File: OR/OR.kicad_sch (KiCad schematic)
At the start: 7 parts, among them J1 AudioJack2_SwitchT, J2 AudioJack2_SwitchT, J3 AudioJack2_SwitchT, Q1 BSS84, Q2 BSS84, Q3 BSS84, Q4 BSS84

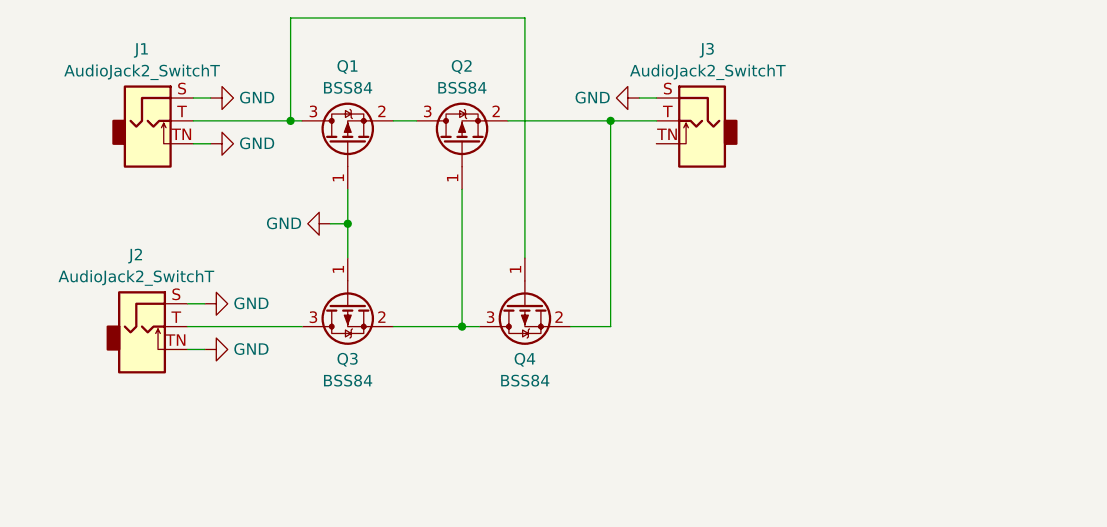
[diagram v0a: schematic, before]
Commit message: Make OR gate lossless
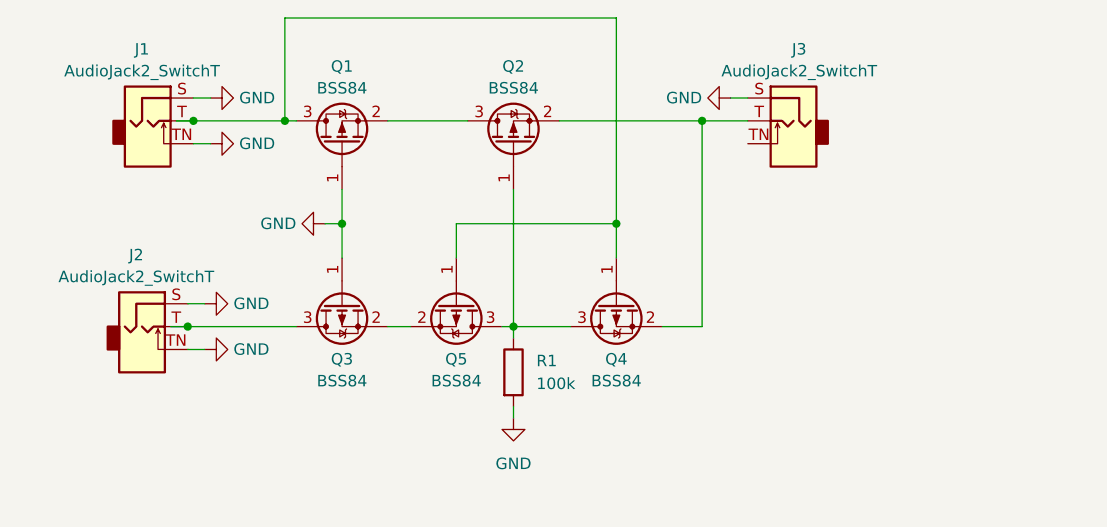
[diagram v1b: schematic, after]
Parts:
- added Q5: BSS84, Package_TO_SOT_SMD:SOT-23, symbol Transistor_FET:BSS84
- added R1: 100k, symbol Device:R
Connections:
- net GND: now also R1.2
- net at J1.T, Q1.3 (D), Q4.1 (G): now also Q5.1 (G)
- net at Q2.1 (G), Q4.3 (D): now also Q5.3 (D), R1.1; no longer Q3.2 (S)
- new net: Q3.2 (S), Q5.2 (S)
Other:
- moved on the sheet: J3, Q1, Q2, Q3, Q4

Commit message: Increase impedance
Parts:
- R1: value 100k -> 1M
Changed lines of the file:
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@@
       (effects (font (size 1.27 1.27)) (justify left))
     )
-    (property "Value" "100k" (at 168.91 96.52 0)
+    (property "Value" "1M" (at 168.91 96.52 0)
       (effects (font (size 1.27 1.27)) (justify left))
     )

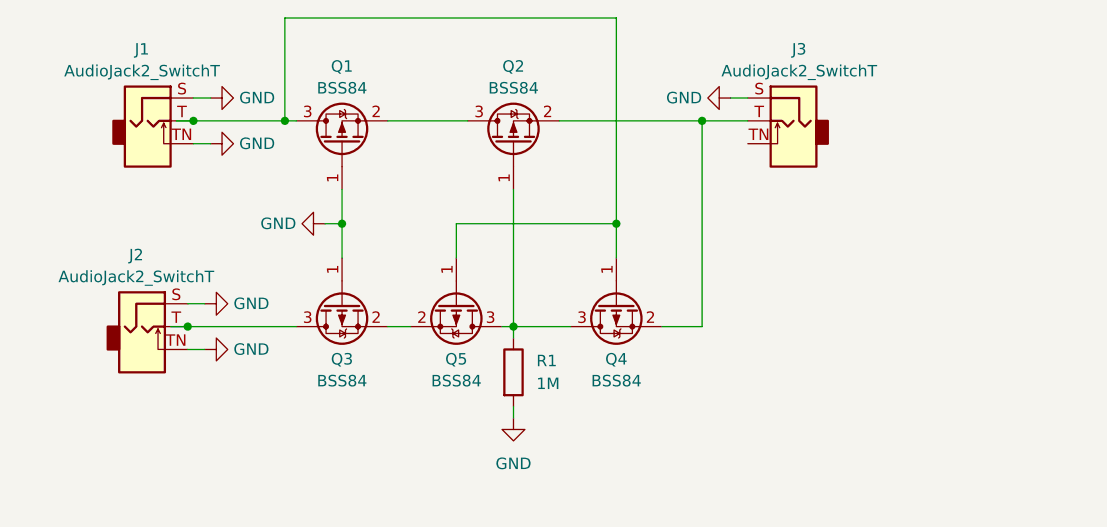
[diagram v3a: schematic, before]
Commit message: Layout OR gate
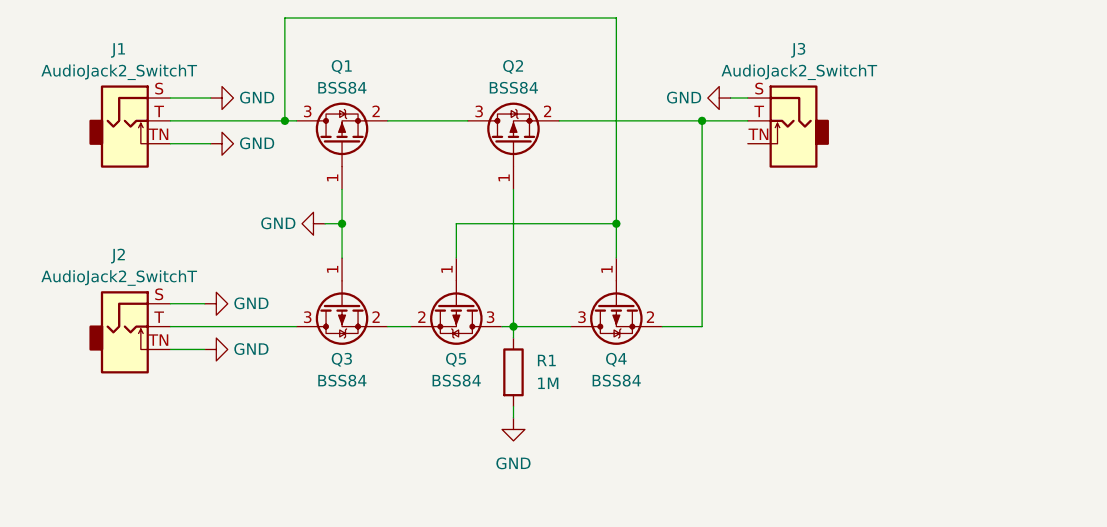
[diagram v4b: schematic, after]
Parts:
- J1, J2, J3: footprint (none) -> Custom_FP:PJ398SM
- R1: footprint (none) -> Resistor_SMD:R_0603_1608Metric
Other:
- moved on the sheet: J1, J2
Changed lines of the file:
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@@
-	)
-	(junction
-		(at 130.81 67.31)
-		(diameter 0)
-		(color 0 0 0 0)
 	)
 	(junction
@@
 	)
 	(junction
-		(at 130.175 90.17)
-		(diameter 0)
-		(color 0 0 0 0)
-	)
-	(junction
 		(at 177.8 78.74)
 		(diameter 0)
@@
 	(wire
 		(pts
-			(xy 130.175 92.71) (xy 132.08 92.71)
+			(xy 128.27 92.71) (xy 132.08 92.71)
 		)
 		(stroke
@@
 	(wire
 		(pts
-			(xy 130.81 64.77) (xy 132.715 64.77)
+			(xy 128.27 64.77) (xy 132.715 64.77)
 		)
 		(stroke
@@
 	(wire
 		(pts
-			(xy 130.175 87.63) (xy 132.08 87.63)
+			(xy 128.27 87.63) (xy 132.08 87.63)
 		)
 		(stroke
@@
 	(wire
 		(pts
+			(xy 128.27 67.31) (xy 140.97 67.31)
+		)
+		(stroke
+			(width 0)
+			(type default)
+		)
+	)
+	(wire
+		(pts
 			(xy 187.325 67.31) (xy 187.325 90.17)
 		)
@@
 	(wire
 		(pts
-			(xy 128.905 67.31) (xy 130.81 67.31)
-		)
-		(stroke
-			(width 0)
-			(type default)
-		)
-	)
-	(wire
-		(pts
 			(xy 187.325 67.31) (xy 192.405 67.31)
 		)
@@
 	(wire
 		(pts
-			(xy 130.81 67.31) (xy 140.97 67.31)
-		)
-		(stroke
-			(width 0)
-			(type default)
-		)
-	)
-	(wire
-		(pts
 			(xy 166.37 99.06) (xy 166.37 100.33)
 		)
@@
 	(wire
 		(pts
-			(xy 130.175 90.17) (xy 142.24 90.17)
-		)
-		(stroke
-			(width 0)
-			(type default)
-		)
-	)
-	(wire
-		(pts
-			(xy 128.27 90.17) (xy 130.175 90.17)
+			(xy 128.27 90.17) (xy 142.24 90.17)
 		)
 		(stroke
@@
 	(wire
 		(pts
-			(xy 130.81 69.85) (xy 132.715 69.85)
+			(xy 128.27 69.85) (xy 132.715 69.85)
 		)
 		(stroke
@@
 	(symbol
 		(lib_id "Connector_Audio:AudioJack2_SwitchT")
-		(at 125.095 90.17 0)
+		(at 123.19 90.17 0)
 		(unit 1)
 		(exclude_from_sim no)
@@
 		(fields_autoplaced yes)
 		(property "Reference" "J2"
-			(at 124.46 82.2157 0)
+			(at 122.555 82.2157 0)
 			(effects
 				(font
@@
 		)
 		(property "Value" "AudioJack2_SwitchT"
-			(at 124.46 84.6399 0)
-			(effects
-				(font
-					(size 1.27 1.27)
-				)
-			)
-		)
-		(property "Footprint" ""
-			(at 125.095 90.17 0)
+			(at 122.555 84.6399 0)
+			(effects
+				(font
+					(size 1.27 1.27)
+				)
+			)
+		)
+		(property "Footprint" "Custom_FP:PJ398SM"
+			(at 123.19 90.17 0)
 			(effects
 				(font
@@
 		)
 		(property "Datasheet" "~"
-			(at 125.095 90.17 0)
-			(effects
-				(font
-					(size 1.27 1.27)
-				)
-				(hide yes)
-			)
-		)
-		(property "Description" ""
-			(at 125.095 90.17 0)
+			(at 123.19 90.17 0)
+			(effects
+				(font
+					(size 1.27 1.27)
+				)
+				(hide yes)
+			)
+		)
+		(property "Description" ""
+			(at 123.19 90.17 0)
 			(effects
 				(font
@@
 			)
 		)
-		(property "Footprint" ""
+		(property "Footprint" "Resistor_SMD:R_0603_1608Metric"
 			(at 164.592 95.25 90)
 			(effects
@@
 	(symbol
 		(lib_id "Connector_Audio:AudioJack2_SwitchT")
-		(at 125.73 67.31 0)
+		(at 123.19 67.31 0)
 		(unit 1)
 		(exclude_from_sim no)
@@
 		(fields_autoplaced yes)
 		(property "Reference" "J1"
-			(at 125.095 59.3557 0)
+			(at 122.555 59.3557 0)
 			(effects
 				(font
@@
 		)
 		(property "Value" "AudioJack2_SwitchT"
-			(at 125.095 61.7799 0)
-			(effects
-				(font
-					(size 1.27 1.27)
-				)
-			)
-		)
-		(property "Footprint" ""
-			(at 125.73 67.31 0)
+			(at 122.555 61.7799 0)
+			(effects
+				(font
+					(size 1.27 1.27)
+				)
+			)
+		)
+		(property "Footprint" "Custom_FP:PJ398SM"
+			(at 123.19 67.31 0)
 			(effects
 				(font
@@
 		)
 		(property "Datasheet" "~"
-			(at 125.73 67.31 0)
-			(effects
-				(font
-					(size 1.27 1.27)
-				)
-				(hide yes)
-			)
-		)
-		(property "Description" ""
-			(at 125.73 67.31 0)
+			(at 123.19 67.31 0)
+			(effects
+				(font
+					(size 1.27 1.27)
+				)
+				(hide yes)
+			)
+		)
+		(property "Description" ""
+			(at 123.19 67.31 0)
 			(effects
 				(font
@@
 			)
 		)
-		(property "Footprint" ""
+		(property "Footprint" "Custom_FP:PJ398SM"
 			(at 197.485 67.31 0)
 			(effects

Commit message: Add pulldown when OR inputs are low
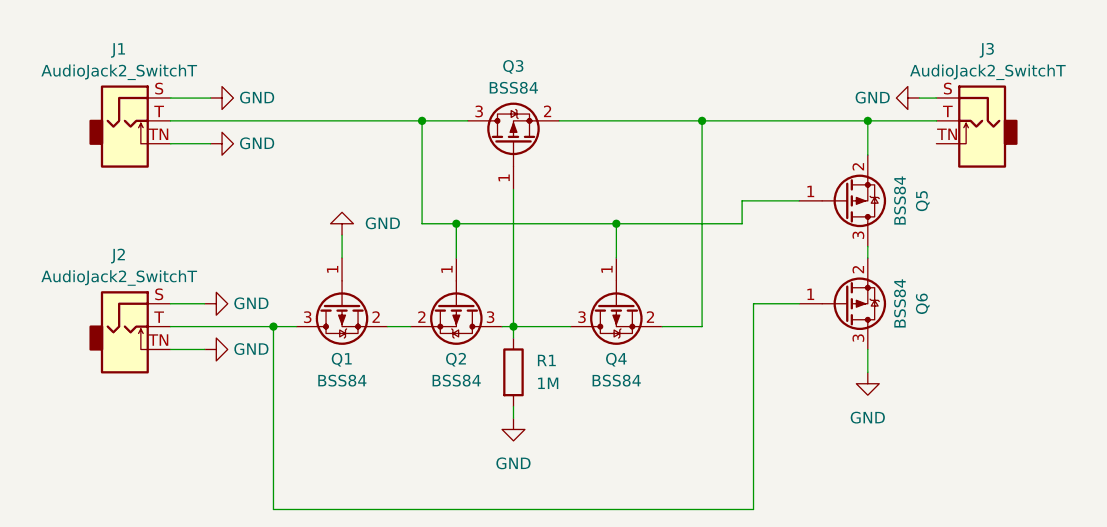
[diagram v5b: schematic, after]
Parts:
- removed Q1: BSS84, Package_TO_SOT_SMD:SOT-23, symbol Transistor_FET:BSS84
- added Q5, Q6: BSS84, Package_TO_SOT_SMD:SOT-23, symbol Transistor_FET:BSS84
- renumbered Q3 to Q1, Q5 to Q2, Q2 to Q3
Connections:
- net GND: now also Q6.3 (D)
- net at J1.T, Q2.1 (G), Q4.1 (G): now also Q3.3 (D), Q5.1 (G)
- net at J2.T, Q1.3 (D): now also Q6.1 (G)
- net at J3.T, Q3.2 (S), Q4.2 (S): now also Q5.2 (S)
- new net: Q5.3 (D), Q6.2 (S)
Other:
- moved on the sheet: J3
